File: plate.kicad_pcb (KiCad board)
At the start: 2 copper layers, 114.3 x 95.3 mm, 0 parts

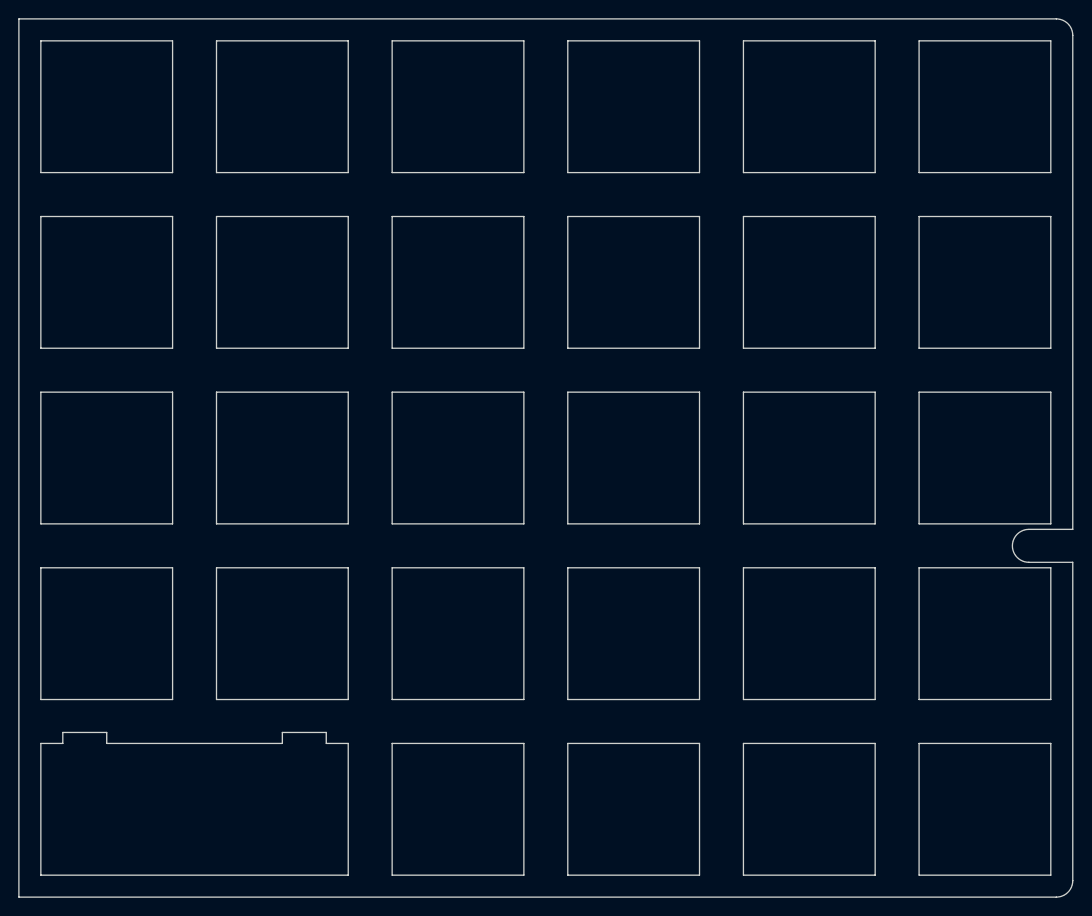
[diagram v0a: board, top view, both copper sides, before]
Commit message: Add copper layer to plate PCB
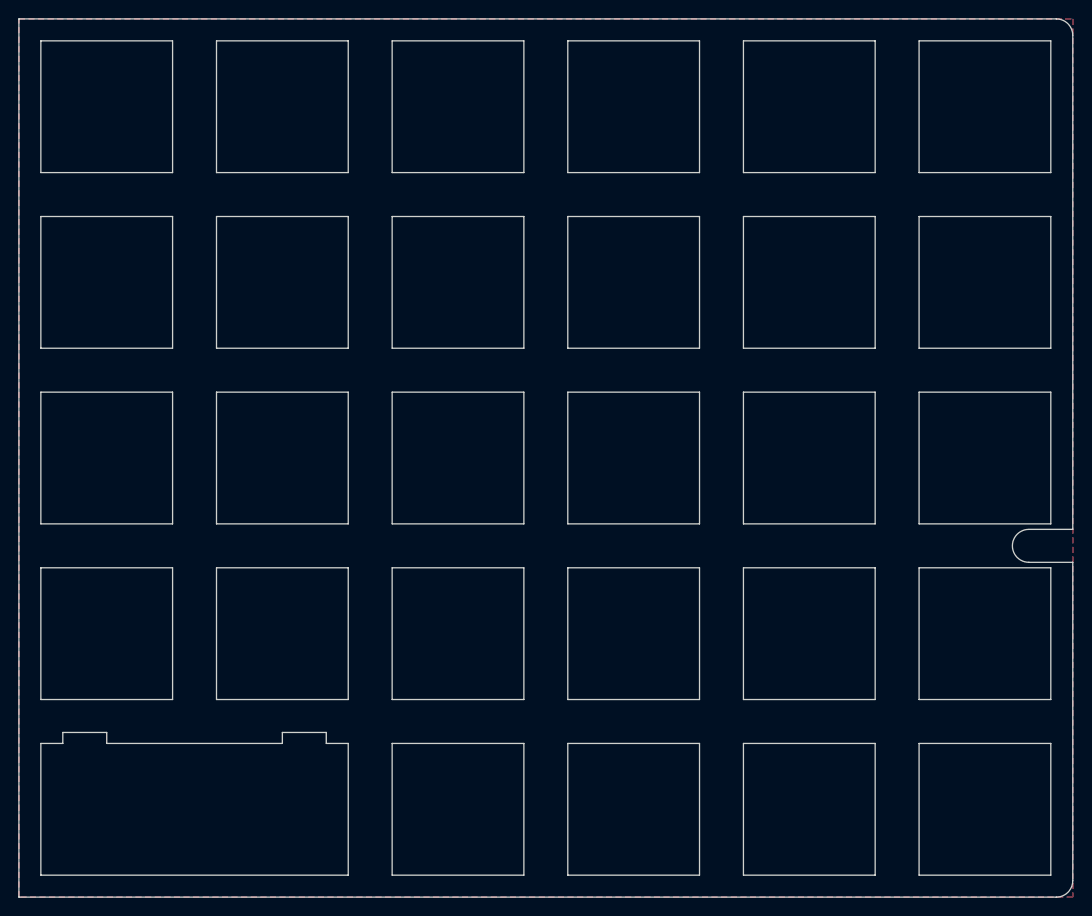
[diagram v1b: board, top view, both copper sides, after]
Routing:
- added copper zone on B.Cu, net (none)
- added copper zone on F.Cu, net (none)
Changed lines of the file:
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@@
     (0 F.Cu signal)
     (31 B.Cu signal)
-    (32 B.Adhes user)
-    (33 F.Adhes user)
-    (34 B.Paste user)
-    (35 F.Paste user)
-    (36 B.SilkS user)
-    (37 F.SilkS user)
-    (38 B.Mask user)
-    (39 F.Mask user)
-    (40 Dwgs.User user)
-    (41 Cmts.User user)
-    (42 Eco1.User user)
-    (43 Eco2.User user)
+    (32 B.Adhes user hide)
+    (33 F.Adhes user hide)
+    (34 B.Paste user hide)
+    (35 F.Paste user hide)
+    (36 B.SilkS user hide)
+    (37 F.SilkS user hide)
+    (38 B.Mask user hide)
+    (39 F.Mask user hide)
+    (40 Dwgs.User user hide)
+    (41 Cmts.User user hide)
+    (42 Eco1.User user hide)
+    (43 Eco2.User user hide)
     (44 Edge.Cuts user)
-    (45 Margin user)
-    (46 B.CrtYd user)
-    (47 F.CrtYd user)
-    (48 B.Fab user)
-    (49 F.Fab user)
+    (45 Margin user hide)
+    (46 B.CrtYd user hide)
+    (47 F.CrtYd user hide)
+    (48 B.Fab user hide)
+    (49 F.Fab user hide)
   )
   (setup
@@
     (visible_elements FFFFF77F)
     (pcbplotparams
-      (layerselection 0x010fc_ffffffff)
+      (layerselection 0x010ff_ffffffff)
       (usegerberextensions true)
-      (usegerberattributes true)
-      (usegerberadvancedattributes true)
-      (creategerberjobfile true)
+      (usegerberattributes false)
+      (usegerberadvancedattributes false)
+      (creategerberjobfile false)
       (excludeedgelayer true)
       (linewidth 0.100000)
@@
   (gr_arc (start 214.907993 143.470433) (end 214.907993 145.256372) (angle -90) (layer Edge.Cuts) (width 0.1))
   (gr_arc (start 214.907993 51.792231) (end 216.693932 51.792231) (angle -90) (layer Edge.Cuts) (width 0.1))
+  (zone (net 0) (net_name "") (layer F.Cu) (hatch edge 0.508)
+    (connect_pads (clearance 0.508))
+    (min_thickness 0.254)
+    (fill yes (arc_segments 32) (thermal_gap 0.508) (thermal_bridge_width 0.508))
+    (polygon
+      (pts
+        (xy 216.693932 145.256372) (xy 102.393836 145.256372) (xy 102.393836 50.006292) (xy 216.693932 50.006292)
+      )
+    )
+  )
+  (zone (net 0) (net_name "") (layer B.Cu) (hatch edge 0.508)
+    (connect_pads (clearance 0.508))
+    (min_thickness 0.254)
+    (fill yes (arc_segments 32) (thermal_gap 0.508) (thermal_bridge_width 0.508))
+    (polygon
+      (pts
+        (xy 216.693932 145.256372) (xy 102.393836 145.256372) (xy 102.393836 50.006292) (xy 216.693932 50.006292)
+      )
+    )
+  )
 )
